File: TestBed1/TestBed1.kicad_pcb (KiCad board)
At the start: 2 copper layers, 44 parts, among them J1 X27Motor, J10 DisplaySegment, J3 X27Motor, J4 X27Motor, J5 TAG_CONNECT, J6 Conn_01x02_Pin, J7 Conn_01x02_Pin, J8 Conn_01x02_Pin, J9 Conn_01x02_Pin, U1 STM32G0B1KBTx, U2 MCP2562-E-SN, U3 TLC5973, U4 TPS54308, U5 MIC5365-3.3YC5, U6 TXB0101DBV

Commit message: WIP Further Grouping
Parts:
- moved D1 160.4 mm to (72.7, 59.9)
- moved J9 160.4 mm to (77.9, 57.3)
- moved D3 146.6 mm to (108.2, 94.3)
- moved J8 146.6 mm to (113.2, 92.5)
- moved J7 88.3 mm to (148.3, 53.5), turned to -90 degrees
- moved D2 85.7 mm to (146.7, 49.8)
- moved C2 17.0 mm to (225.2, 42.9), turned to 90 degrees
- moved C1 16.4 mm to (231.5, 70.9), turned to 90 degrees
- moved R5 15.7 mm to (216.8, 45.8), turned to -90 degrees
- moved TP6 13.9 mm to (231.2, 68.6), turned to 90 degrees
- moved TP5 13.5 mm to (231.2, 73.2), turned to 90 degrees
- moved R3 12.6 mm to (209.5, 83.8)
- moved C4 12.0 mm to (168.0, 67.7), turned to -90 degrees
- moved TP2 11.4 mm to (241.0, 72.0), turned to 180 degrees
- moved R2 11.0 mm to (227.6, 46.1)
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
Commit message: Schematic Assignment, board assignemtn and rough placement
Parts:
- removed J7, J8, J9: Conn_01x02_Pin, Connector_PinHeader_2.54mm:PinHeader_1x02_P2.54mm_Vertical
- added C8: 0.1u, Capacitor_SMD:C_0402_1005Metric_Pad0.74x0.62mm_HandSolder, F.Cu at (173.6, 121.8)
- added D5: LED, LED_SMD:LED_Luminus_MP-3030-1100_3.0x3.0mm, F.Cu at (81.9, 122.9)
- added D6: LED, LED_SMD:LED_Luminus_MP-3030-1100_3.0x3.0mm, F.Cu at (78.1, 122.9)
- added D7: LED, LED_SMD:LED_Luminus_MP-3030-1100_3.0x3.0mm, F.Cu at (74.2, 122.9)
- added H1: MountingHole, MountingHole:MountingHole_3.2mm_M3, F.Cu at (266.2, 33.6)
- added H2: MountingHole, MountingHole:MountingHole_3.2mm_M3, F.Cu at (266.2, 41.5)
- added H3: MountingHole, MountingHole:MountingHole_3.2mm_M3, F.Cu at (266.2, 49.5)
- added H4: MountingHole, MountingHole:MountingHole_3.2mm_M3, F.Cu at (266.2, 57.4)
- added J2: Conn_01x04_Pin, X27:CONN_70551-xxxx_04_MOL, B.Cu at (139.2, 94.0)
- added L1: 12u, Inductor_SMD:L_1812_4532Metric, F.Cu at (211.1, 91.7)
- added R10: 0, Resistor_SMD:R_0402_1005Metric, F.Cu at (228.9, 68.8)
- added R11: 0, Resistor_SMD:R_0402_1005Metric, F.Cu at (228.9, 72.9)
- added R12: 0, Resistor_SMD:R_0402_1005Metric, F.Cu at (186.4, 108.6)
- added R13: 0, Resistor_SMD:R_0402_1005Metric, F.Cu at (186.4, 110.6)
- added R14: 1.5k, Resistor_SMD:R_0402_1005Metric, F.Cu at (186.3, 66.5)
- added R15: 250, Resistor_SMD:R_0402_1005Metric, F.Cu at (184.0, 67.8)
- added R8: 0, Resistor_SMD:R_0402_1005Metric, F.Cu at (228.9, 67.6)
- added R9: 0, Resistor_SMD:R_0402_1005Metric, F.Cu at (228.9, 74.2)
- added TP7: TestPoint, TestPoint:TestPoint_Pad_1.0x1.0mm, F.Cu at (166.6, 69.1)
- added U7: ~, X27:SFH_5711-23-Z, F.Cu at (207.6, 113.3)
- added U8: MCP2515-xSO, Package_SO:SOIC-18W_7.5x11.6mm_P1.27mm, F.Cu at (178.5, 114.3)
- J5: moved to B.Cu
- moved D2 90.6 mm to (93.4, 122.9)
- moved D1 64.4 mm to (85.7, 122.9)
- moved J5 42.4 mm to (189.7, 33.4), turned to 180 degrees
- moved D3 34.2 mm to (89.5, 122.9)
- moved J1 11.5 mm to (117.0, 53.7), turned to -45 degrees
- moved J4 11.1 mm to (66.0, 54.1), turned to 45 degrees
- moved D4 2.66 mm to (186.7, 67.8)
- moved R7 2.66 mm to (189.8, 67.8)
- moved C4 0.56 mm to (167.4, 67.6), turned to 180 degrees
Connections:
- D4 pad 1: /LEDs/HB_LED -> Net-(D4-K)
- J1 pad 1: /Motors/P1_0 -> /MCU/P1_0
- J1 pad 2: /Motors/P2_0 -> /MCU/P2_0
- J1 pad 3: /Motors/P3_0 -> /MCU/P3_0
- J1 pad 4: /Motors/P4_0 -> /MCU/P4_0
- J3 pad 1: /Motors/P1_1 -> /MCU/P1_1
- J3 pad 2: /Motors/P2_1 -> /MCU/P2_1
- J3 pad 3: /Motors/P3_1 -> /MCU/P3_1
- J3 pad 4: /Motors/P4_1 -> /MCU/P4_1
- J4 pad 1: /Motors/P1_2 -> /MCU/P1_2
- J4 pad 2: /Motors/P2_2 -> /MCU/P2_2
- J4 pad 3: /Motors/P3_2 -> /MCU/P3_2
- J4 pad 4: /Motors/P4_2 -> /MCU/P4_2
- J6 pad 2: /MCU/AMB_OUT -> /LEDs/AMB_OUT
- R6 pad 1: /MCU/AMB_OUT -> /LEDs/AMB_OUT
- U1 pad 1: unconnected-(U1-PB9-Pad1) -> /CANBus/CAN_MCU_TXD
- U1 pad 10: unconnected-(U1-PA3-Pad10) -> /MCU/P1_1
- U1 pad 11: unconnected-(U1-PA4-Pad11) -> /CANBus/CAN_~CS
- U1 pad 12: unconnected-(U1-PA5-Pad12) -> /MCU/P2_1
- U1 pad 13: unconnected-(U1-PA6-Pad13) -> /CANBus/CAN_MISO
- U1 pad 14: unconnected-(U1-PA7-Pad14) -> /MCU/P3_1
- U1 pad 15: unconnected-(U1-PB0-Pad15) -> /MCU/P1_2
- U1 pad 16: unconnected-(U1-PB1-Pad16) -> /MCU/P2_2
- U1 pad 17: unconnected-(U1-PB2-Pad17) -> /MCU/P3_2
- U1 pad 18: unconnected-(U1-PA8-Pad18) -> /CANBus/CAN_STBY
- U1 pad 19: unconnected-(U1-PA9/UCPD1_DBCC1-Pad19) -> /CANBus/CAN_~RST
- U1 pad 2: unconnected-(U1-PC14-Pad2) -> /CANBus/CAN_~RX1BF
- U1 pad 20: unconnected-(U1-PC6-Pad20) -> /CANBus/CAN_~TX0RTS
- U1 pad 21: unconnected-(U1-PA10/UCPD1_DBCC2-Pad21) -> /LEDs/HB_LED
- U1 pad 22: unconnected-(U1-PA9/PA11-Pad22) -> /CANBus/CAN_MCU_RXD
- U1 pad 23: unconnected-(U1-PA10/PA12-Pad23) -> /CANBus/CAN_~INT
- U1 pad 24: unconnected-(U1-PA13-Pad24) -> /MCU/SWDIO
- U1 pad 25: unconnected-(U1-PA14-Pad25) -> /MCU/SWDCLK
- U1 pad 26: unconnected-(U1-PA15-Pad26) -> /MCU/P4_1
- U1 pad 27: unconnected-(U1-PB3-Pad27) -> /MCU/P4_2
- U1 pad 28: unconnected-(U1-PB4-Pad28) -> /MCU/P1_0
- U1 pad 29: unconnected-(U1-PB5-Pad29) -> /MCU/P2_0
- U1 pad 3: unconnected-(U1-PC15-Pad3) -> /CANBus/CAN_~RX0BF
- U1 pad 30: unconnected-(U1-PB6-Pad30) -> /MCU/P3_0
- U1 pad 31: unconnected-(U1-PB7-Pad31) -> /MCU/P4_0
- U1 pad 32: unconnected-(U1-PB8-Pad32) -> /LEDs/LED_IN
- U1 pad 6: unconnected-(U1-PF2-Pad6) -> /CANBus/CAN_MCO
- U1 pad 7: unconnected-(U1-PA0-Pad7) -> /LEDs/AMB_OUT
- U1 pad 8: unconnected-(U1-PA1-Pad8) -> /CANBus/CAN_SCK
- U1 pad 9: unconnected-(U1-PA2-Pad9) -> /CANBus/CAN_MOSI
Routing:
- net Net-(D4-A): track 0.00 -> 1.53 mm

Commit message: WIP placement
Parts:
- C1, C11, C12, C13, C2, C3, C4, C5, C6, C7, C8, C9, D4, J6, JP1, L1, R1, R10, R11, R12, R13, R14, R15, R2, R3, R4, R5, R6, R7, R8, R9, TP1, TP2, TP3, TP4, TP5, TP6, TP7, U1, U2, U3, U4, U5, U6, U8: moved to B.Cu
- moved U7 138.1 mm to (90.2, 40.4)
- moved D3 66.9 mm to (93.0, 56.1), turned to 90 degrees
- moved D5 63.9 mm to (93.0, 60.0), turned to 90 degrees
- moved D1 45.1 mm to (115.3, 88.9), turned to 90 degrees
- moved D6 42.5 mm to (65.0, 82.5), turned to 90 degrees
- moved D7 37.8 mm to (65.0, 86.3), turned to 90 degrees
- moved D2 37.3 mm to (115.3, 92.8), turned to 90 degrees
- moved U8 35.0 mm to (156.5, 87.1), turned to 180 degrees
- moved R7 32.0 mm to (157.8, 67.8), turned to 0 degrees
- moved R2 26.7 mm to (200.8, 46.1), turned to 180 degrees
- moved D4 25.7 mm to (161.0, 67.8), turned to 180 degrees
- moved R14 24.9 mm to (161.4, 66.5), turned to 180 degrees
- moved J2 22.4 mm to (120.9, 81.0)
- moved C2 22.1 mm to (203.2, 42.9)
- moved R15 20.4 mm to (163.6, 67.8), turned to 180 degrees
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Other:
- board outline added: 81.3 x 60.2 mm

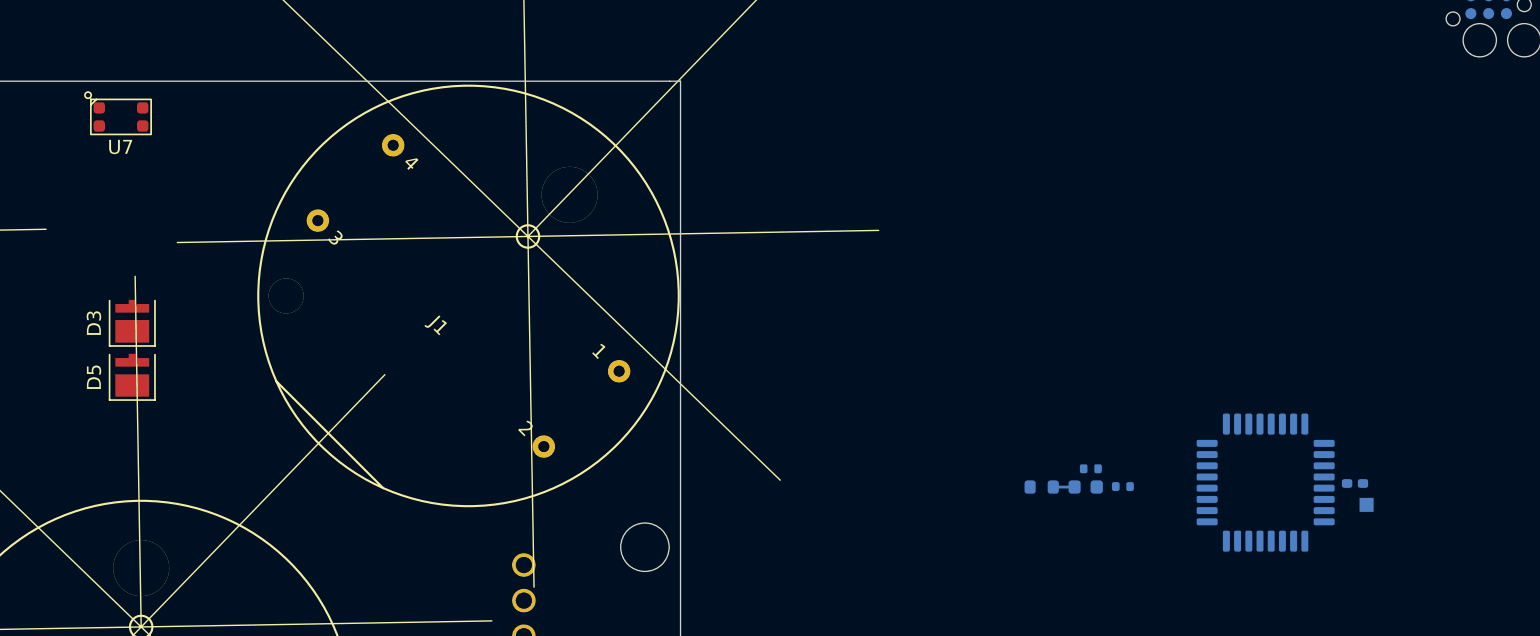
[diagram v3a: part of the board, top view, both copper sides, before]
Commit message: Board Outline and Connector Placement
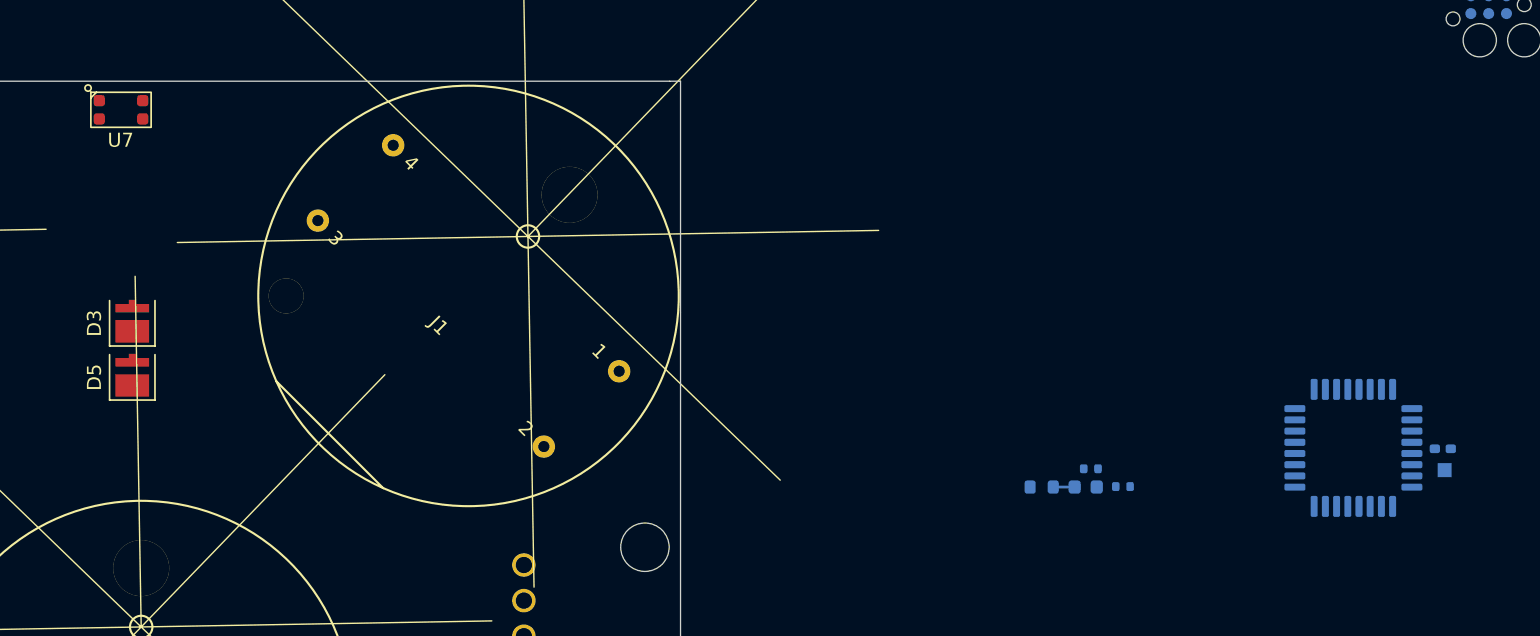
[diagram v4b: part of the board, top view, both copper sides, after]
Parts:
- moved U1 6.73 mm to (180.1, 65.0)
- moved C4 6.73 mm to (186.5, 65.1)
- moved TP7 6.10 mm to (186.6, 66.6)
- moved U7 0.51 mm to (90.2, 39.9)
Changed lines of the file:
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@@
 	(footprint "X27:SFH_5711-23-Z"
 		(layer "F.Cu")
-		(at 90.209804 40.359804)
+		(at 90.209804 39.851804)
 		(property "Reference" "U7"
 			(at 1.924 3.224 0)
@@
 	(footprint "Package_QFP:LQFP-32_7x7mm_P0.8mm"
 		(layer "B.Cu")
-		(at 173.825 67.5 180)
+		(at 180.086 65.024 180)
 		(descr "LQFP, 32 Pin (https://www.nxp.com/docs/en/package-information/SOT358-1.pdf), generated with kicad-footprint-generator ipc_gullwing_generator.py")
 		(tags "LQFP QFP")
@@
 	(footprint "Capacitor_SMD:C_0402_1005Metric_Pad0.74x0.62mm_HandSolder"
 		(layer "B.Cu")
-		(at 180.2045 67.564)
+		(at 186.4655 65.088)
 		(descr "Capacitor SMD 0402 (1005 Metric), square (rectangular) end terminal, IPC_7351 nominal with elongated pad for handsoldering. (Body size source: IPC-SM-782 page 76, https://www.pcb-3d.com/wordpress/wp-content/uploads/ipc-sm-782a_amendment_1_and_2.pdf), generated with kicad-footprint-generator")
 		(tags "capacitor handsolder")
@@
 	(footprint "TestPoint:TestPoint_Pad_1.0x1.0mm"
 		(layer "B.Cu")
-		(at 181.026 69.088 90)
+		(at 186.601 66.612 90)
 		(descr "SMD rectangular pad as test Point, square 1.0mm side length")
 		(tags "test point SMD pad rectangle square")

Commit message: WIP need layout and reconfiguring
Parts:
- added D10: LED, LED_SMD:LED_Luminus_MP-3030-1100_3.0x3.0mm, F.Cu at (167.9, 33.6)
- added D8: LED, LED_SMD:LED_Luminus_MP-3030-1100_3.0x3.0mm, F.Cu at (156.3, 40.1)
- added D9: LED, LED_SMD:LED_Luminus_MP-3030-1100_3.0x3.0mm, F.Cu at (162.3, 24.5)
- J10: footprint Library:DisplayPassthrough -> X27:DisplayPassthrough
- moved C13 189.0 mm to (32.3, 90.6), turned to 180 degrees
- moved C12 187.4 mm to (32.3, 92.9), turned to 180 degrees
- moved U6 184.8 mm to (35.1, 91.8), turned to -90 degrees
- moved R5 183.5 mm to (34.6, 94.4), turned to 0 degrees
- moved C2 182.8 mm to (33.2, 110.2), turned to 180 degrees
- moved TP3 182.2 mm to (37.9, 90.7), turned to 90 degrees
- moved TP4 180.7 mm to (37.9, 92.8), turned to 90 degrees
- moved U3 179.2 mm to (37.1, 107.7), turned to -90 degrees
- moved R2 177.3 mm to (36.4, 112.5), turned to -90 degrees
- moved J5 154.1 mm to (60.5, 117.4), turned to -45 degrees
- moved R15 135.3 mm to (32.3, 35.2), turned to -135 degrees
- moved R14 135.1 mm to (29.8, 35.9), turned to -135 degrees
- moved D4 134.1 mm to (30.4, 37.1), turned to -135 degrees
- moved R7 132.7 mm to (28.2, 39.4), turned to 45 degrees
- moved U1 127.1 mm to (67.6, 124.2)
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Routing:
- net GND: track 0.00 -> 30.9 mm, vias 0 -> 21
- net +3V3: track 0.00 -> 9.97 mm, vias 0 -> 1
- net +5V: track 0.00 -> 6.70 mm
- net Net-(U4-SW): track 0.00 -> 6.56 mm
- net /CAN_VCC: track 0.00 -> 6.17 mm
- net /CANBus/CAN_RXD: track 0.00 -> 6.07 mm
- net /CANBus/CAN_TXD: track 0.00 -> 6.03 mm
- net /CANH: track 0.00 -> 5.36 mm
- net /CANL: track 0.00 -> 4.95 mm
- net /MCU/SWDIO: track 0.00 -> 4.88 mm
- net /MCU/SWDCLK: track 0.00 -> 4.88 mm
- net /LEDs/AMB_OUT: track 0.00 -> 4.32 mm, vias 0 -> 1
- net /CANBus/CAN_MCU_TXD: track 0.00 -> 3.33 mm
- net Net-(U4-FB): track 0.00 -> 2.74 mm
- net Net-(D4-K): track 0.00 -> 2.72 mm
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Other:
- board size 81.3 x 60.2 mm -> 81.3 x 67.8 mm

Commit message: Rough Placement and board outline
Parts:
- removed H1, H2, H3, H4: MountingHole, MountingHole:MountingHole_3.2mm_M3
- removed J10: DisplaySegment, X27:DisplayPassthrough
- added J7: Conn_01x02_Pin, Connector_PinHeader_1.27mm:PinHeader_1x02_P1.27mm_Vertical, B.Cu at (146.6, 106.1)
- moved D1 114.7 mm to (84.3, 113.6), turned to -90 degrees
- moved D9 104.5 mm to (108.1, 113.8), turned to -90 degrees
- moved D7 102.6 mm to (81.4, 100.0), turned to 180 degrees
- moved J6 97.7 mm to (151.5, 104.5)
- moved C11 97.7 mm to (146.7, 102.8)
- moved U7 97.7 mm to (144.6, 101.7)
- moved R6 97.7 mm to (149.9, 102.2)
- moved D10 87.0 mm to (135.1, 114.2), turned to -90 degrees
- moved R15 84.2 mm to (98.1, 87.8), turned to 180 degrees
- moved R14 83.1 mm to (95.8, 86.5), turned to 180 degrees
- moved D4 82.4 mm to (95.4, 87.8), turned to 180 degrees
- moved D2 81.4 mm to (159.8, 113.9), turned to -90 degrees
- moved R7 80.3 mm to (92.3, 87.8), turned to 0 degrees
- moved D5 72.4 mm to (173.4, 105.6), turned to 0 degrees
- moved C6 67.5 mm to (104.9, 103.9), turned to 90 degrees
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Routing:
- net /CANBus/CAN_MCU_RXD: track 0.00 -> 13.8 mm
- net /CANBus/CAN_MCU_TXD: track 3.33 -> 14.4 mm
- net /CANBus/CAN_TXD: track 6.03 -> 15.2 mm, vias 0 -> 2
- net /CANBus/CAN_RXD: track 6.07 -> 13.1 mm, vias 0 -> 2
- net +3V3: track 9.97 -> 15.6 mm
- net /LEDs/AMB_OUT: track 4.32 -> 8.64 mm
- net /LEDs/LED_OUT: track 1.84 -> 5.81 mm
- net /CANBus/CAN_MCO: track 2.50 -> 0.55 mm
- net GND: track 30.9 -> 32.6 mm, vias 21 -> 22
- net /MCU/SWDIO: track 4.88 -> 3.20 mm
- net /MCU/SWDCLK: track 4.88 -> 3.46 mm
- net /CANH: track 5.36 -> 4.82 mm
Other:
- board size 81.3 x 67.8 mm -> 98.4 x 44.2 mm

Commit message: WIP - routing
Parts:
- moved R6 2.37 mm to (151.2, 104.2)
- moved U7 2.37 mm to (145.9, 103.7)
- moved C11 2.37 mm to (148.0, 104.8)
- moved J6 2.37 mm to (152.7, 106.5)
- moved J7 2.37 mm to (147.9, 108.1)
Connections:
- J5 pad 1: VCC -> +3V3
- U1 pad 10: /MCU/P1_1 -> unconnected-(U1-PA3-Pad10)
- U1 pad 11: /CANBus/CAN_~CS -> unconnected-(U1-PA4-Pad11)
- U1 pad 12: /MCU/P2_1 -> unconnected-(U1-PA5-Pad12)
- U1 pad 15: /MCU/P1_2 -> /CANBus/CAN_~RX0BF
- U1 pad 16: /MCU/P2_2 -> /CANBus/CAN_~RX1BF
- U1 pad 17: /MCU/P3_2 -> /LEDs/LED_IN
- U1 pad 18: /CANBus/CAN_STBY -> /MCU/P3_2
- U1 pad 19: /CANBus/CAN_~RST -> /MCU/P4_2
- U1 pad 2: /CANBus/CAN_~RX1BF -> unconnected-(U1-PC14-Pad2)
- U1 pad 20: /CANBus/CAN_~TX0RTS -> /LEDs/HB_LED
- U1 pad 21: /LEDs/HB_LED -> /MCU/P1_2
- U1 pad 23: /CANBus/CAN_~INT -> /MCU/P2_2
- U1 pad 26: /MCU/P4_1 -> /MCU/P3_0
- U1 pad 27: /MCU/P4_2 -> /MCU/P4_0
- U1 pad 3: /CANBus/CAN_~RX0BF -> /MCU/P4_1
- U1 pad 30: /MCU/P3_0 -> /CANBus/CAN_~INT
- U1 pad 31: /MCU/P4_0 -> /CANBus/CAN_~RST
- U1 pad 32: /LEDs/LED_IN -> /CANBus/CAN_~TX0RTS
- U3 pad 1: /LEDs/D1 -> /LEDs/D3
- U3 pad 3: /LEDs/D3 -> /LEDs/D1
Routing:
- net +5V: track 6.70 -> 260.5 mm, vias 0 -> 2
- net /LEDs/D3: track 0.00 -> 97.6 mm, vias 0 -> 1
- net /LEDs/D1: track 0.00 -> 85.7 mm, vias 0 -> 1
- net /MCU/P1_0: track 0.00 -> 79.8 mm
- net /MCU/P2_0: track 0.00 -> 67.1 mm
- net /MCU/P4_0: track 0.00 -> 65.2 mm
- net +3V3: track 15.6 -> 76.8 mm, vias 1 -> 5
- net /MCU/P3_0: track 0.00 -> 57.9 mm
- net /LEDs/D2: track 0.00 -> 40.8 mm, vias 0 -> 1
- net /CANBus/CAN_MCU_RXD: track 13.8 -> 46.6 mm, vias 0 -> 2
- net /CANBus/CAN_~TX0RTS: track 0.00 -> 31.4 mm, vias 0 -> 2
- net /CANBus/CAN_MISO: track 0.00 -> 28.3 mm, vias 0 -> 2
- net /CANBus/CAN_~RX0BF: track 0.00 -> 25.6 mm, vias 0 -> 2
- net /CANBus/CAN_~RST: track 0.00 -> 25.4 mm, vias 0 -> 2
- net /CANBus/CAN_~RX1BF: track 0.00 -> 23.9 mm
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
